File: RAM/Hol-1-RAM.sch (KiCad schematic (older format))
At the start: 22 parts, among them P1 ADDRESS PORT, P2 DATA PORT, P3 DATA BUS, P4 Power, U1 74LS139, U10 74LS04, U11 74LS04, U12 74LS245, U2 74LS189, U3 74LS189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

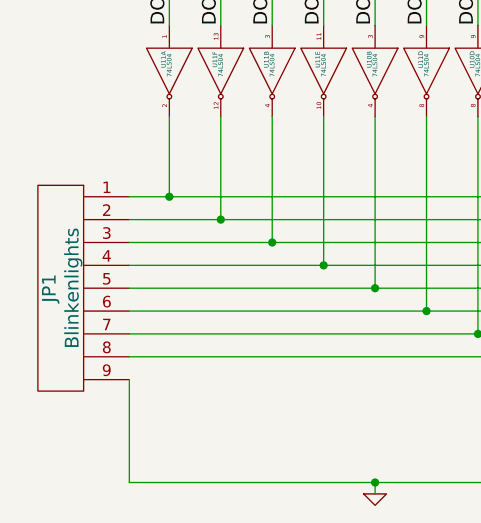
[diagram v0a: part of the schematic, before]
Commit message: v1.0.4 rotated blinkenlight plugin to identify GND
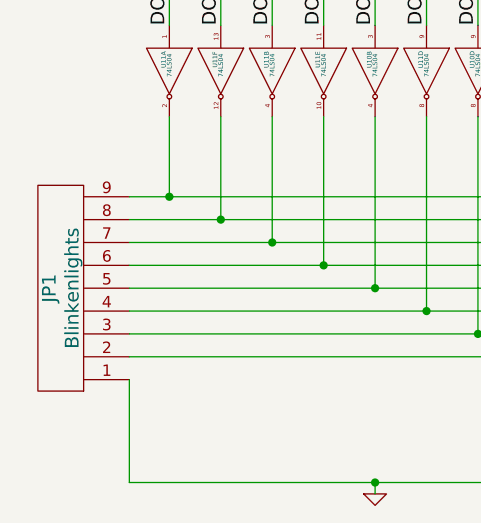
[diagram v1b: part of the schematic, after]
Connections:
- net GND: now also JP1.1 (pin1); no longer JP1.9 (pin9)
- net at U11.2, U12.2 (A1): now also JP1.9 (pin9); no longer JP1.1 (pin1)
- net at U11.12, U12.3 (A2): now also JP1.8 (pin8); no longer JP1.2 (pin2)
- net at U11.4, U12.4 (A3): now also JP1.7 (pin7); no longer JP1.3 (pin3)
- net at U11.10, U12.5 (A4): now also JP1.6 (pin6); no longer JP1.4 (pin4)
- net at U11.8, U12.7 (A6): now also JP1.4 (pin4); no longer JP1.6 (pin6)
- net at U10.8, U12.8 (A7): now also JP1.3 (pin3); no longer JP1.7 (pin7)
- net at U10.6, U12.9 (A8): now also JP1.2 (pin2); no longer JP1.8 (pin8)
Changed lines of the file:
@@
 LIBS:contrib
 LIBS:valves
+LIBS:Hol-1-RAM-cache
 EELAYER 27 0
 EELAYER END
@@
 Sheet 1 1
 Title "Hol-1 8-bit CPU - RAM board"
-Date "28 feb 2019"
+Date "7 mar 2019"
 Rev "1.0"
 Comp "www.Benningtons.Net"
@@
 F 3 "" H 825 6775 60  0000 C CNN
 	1    825  6775
-	0    1    1    0
+	0    1    -1   0
 $EndComp
 Wire Wire Line
@@
 Wire Wire Line
 	1075 7625 3650 7625
-Wire Wire Line
-	1075 7175 1075 7625
 Wire Wire Line
 	2150 7675 2150 7625
@@
 	-1   0    0    -1
 $EndComp
+Wire Wire Line
+	1075 7175 1075 7625
 $EndSCHEMATC

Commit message: v1.1.2 comments added to schematic
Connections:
- net GND: no longer C1.2, C2.2, C3.2, C4.2, P4.2 (PM), U10.7 (GND), U11.7 (GND)
- new net: C1.2, C2.2, C3.2, C4.2, P4.2 (PM), U10.7 (GND), U11.7 (GND)
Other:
- note added: "+5v supply to power rails, to ICs shown as\nlogic symbols within the schematic and to\ndecoupling capacitors."
- note added: "A 16 pin IDC ribbon cable header is wired in\nparallel to provide an 8-bit Data bus."
- note added: "Because the 74LS189 inverts stored data\nthese inverters (left) re-invert the data to output the original."
- note added: "Can't have too\nmany blinking\nLEDs (below)"
- note added: "Control Signals\n-------------------\nRAM-IN: Store input data into selected memory address\nRAM-OUT: Place content of selected memorey address onto Data Bus"
- note added: "Data input bus"
- note added: "Data output bus"
- note added: "Decode the top two bits of the memory\naddress to determine which of the 4\nmemory banks to select."
- note added: "Four vertical pairs of memory banks (below), each holding 16 bytes."
- note added: "Memory address bus"

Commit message: v1.5.19 upgraded to KiCad 5.0
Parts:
- C1, C2, C3, C4, C5: symbol C -> benningtons:C
- JP1: symbol 9-PIN_HEADER -> benningtons:9-PIN_HEADER
- P1, P2: symbol CONN_8 -> benningtons:CONN_8
- P3: symbol CONN_8X2 -> benningtons:CONN_8X2
- P4: symbol CONN_2 -> benningtons:CONN_2
- U1: symbol 74LS139 -> benningtons:74LS139
- U10, U11: symbol 74LS04 -> benningtons:74LS04
- U12: symbol 74LS245 -> benningtons:74LS245
- U2, U3, U4, U5, U6, U7, U8, U9: symbol 74LS189 -> benningtons:74LS189
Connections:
- net GND: now also C1.2, C2.2, C3.2, C4.2, P4.2 (PM), U10.7 (GND), U11.7 (GND)
